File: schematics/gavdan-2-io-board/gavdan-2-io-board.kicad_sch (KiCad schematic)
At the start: 13 parts, among them J1 DB9_Female, U1 74LS04, U2 74LS133, U3 74LS08, U4 74LS08, U5 6551 ACIA, U6 MAX233CPP, U7 6522 VIA, Y1 1.8432MHZ

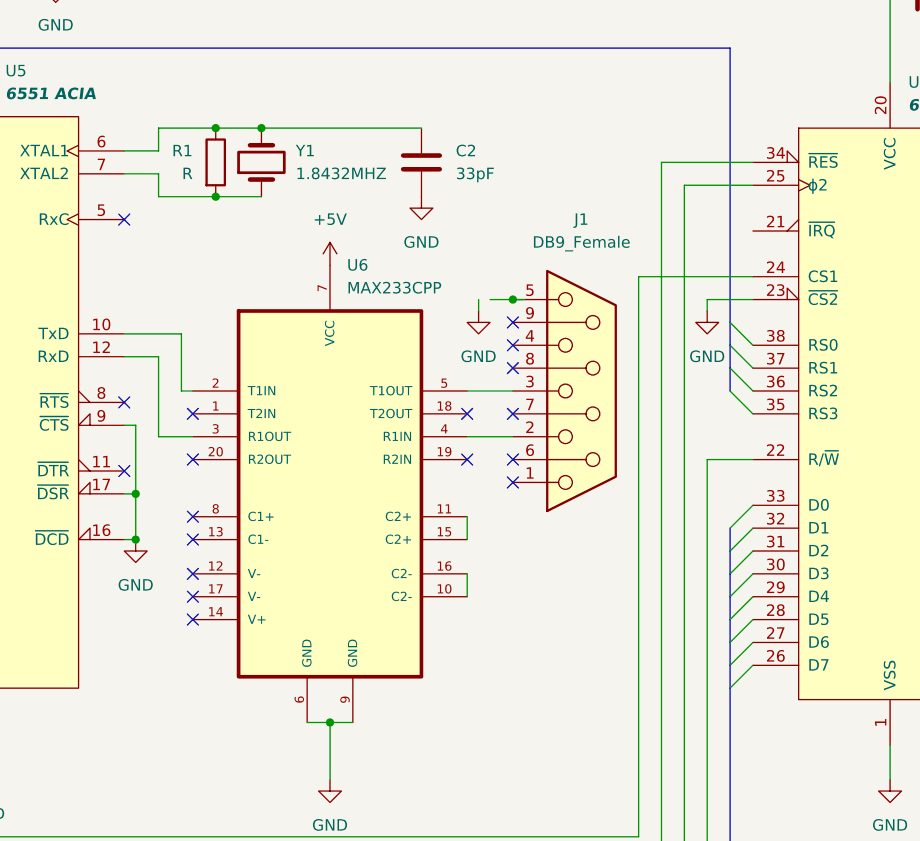
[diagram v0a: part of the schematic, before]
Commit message: Minor errors on schematics corrected
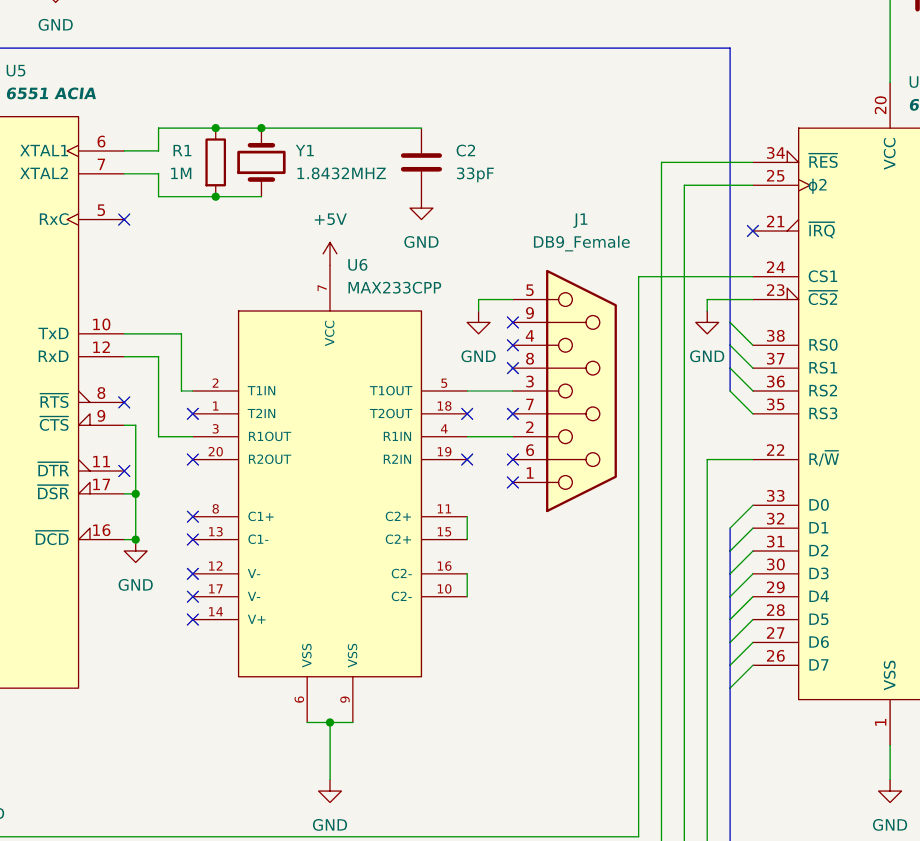
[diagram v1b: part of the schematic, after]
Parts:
- R1: value R -> 1M
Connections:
- net GND: now also J1.5
- no-connect marks 31 -> 32
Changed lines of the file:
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@@
   (junction (at 175.26 45.72) (diameter 0) (color 0 0 0 0)
-  )
-  (junction (at 208.28 64.77) (diameter 0) (color 0 0 0 0)
   )
   (junction (at 129.54 135.89) (diameter 0) (color 0 0 0 0)
@@
   (no_connect (at 165.1 76.2))
   (no_connect (at 165.1 55.88))
+  (no_connect (at 234.95 57.15))
   (no_connect (at 208.28 85.09))
   (no_connect (at 208.28 72.39))
@@
     (stroke (width 0) (type default) (color 0 0 0 0))
   )
-  (wire (pts (xy 208.28 64.77) (xy 209.55 64.77))
-    (stroke (width 0) (type default) (color 0 0 0 0))
-  )
   (bus (pts (xy 41.91 39.37) (xy 41.91 36.83))
     (stroke (width 0) (type default) (color 0 0 0 0))
@@
     (stroke (width 0) (type default) (color 0 0 0 0))
   )
+  (wire (pts (xy 208.28 64.77) (xy 204.47 64.77))
+    (stroke (width 0) (type default) (color 0 0 0 0))
+  )
   (bus (pts (xy 30.48 180.34) (xy 30.48 176.53))
     (stroke (width 0) (type default) (color 0 0 0 0))
@@
     (stroke (width 0) (type default) (color 0 0 0 0))
   )
-  (wire (pts (xy 205.74 64.77) (xy 208.28 64.77))
-    (stroke (width 0) (type default) (color 0 0 0 0))
-  )
   (wire (pts (xy 44.45 110.49) (xy 77.47 110.49))
     (stroke (width 0) (type default) (color 0 0 0 0))
@@
     (stroke (width 0) (type default) (color 0 0 0 0))
   )
+  (wire (pts (xy 204.47 64.77) (xy 204.47 66.04))
+    (stroke (width 0) (type default) (color 0 0 0 0))
+  )
   (wire (pts (xy 44.45 115.57) (xy 77.47 115.57))
     (stroke (width 0) (type default) (color 0 0 0 0))
@@
   )
   (bus (pts (xy 30.48 83.82) (xy 30.48 87.63))
-    (stroke (width 0) (type default) (color 0 0 0 0))
-  )
-  (wire (pts (xy 204.47 66.04) (xy 204.47 64.77))
     (stroke (width 0) (type default) (color 0 0 0 0))
   )
@@
       (effects (font (size 1.27 1.27)) (justify right))
     )
-    (property "Value" "R" (id 1) (at 172.72 50.7999 0)
+    (property "Value" "1M" (id 1) (at 172.72 50.7999 0)
       (effects (font (size 1.27 1.27)) (justify right))
     )
@@
     )
     (path "/91bc8827-3474-4406-866c-90ffdcf01241"
-      (reference "R1") (unit 1) (value "R") (footprint "")
+      (reference "R1") (unit 1) (value "1M") (footprint "")
     )
     (path "/e349a370-d956-4396-bf48-f79433bb1b93"

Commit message: Corrected error with reversed CS lines
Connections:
- net at U5.2 (CS1): now also U4.8; no longer U3.8
- net at U7.24 (CS1): now also U3.8; no longer U4.8
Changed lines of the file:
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@@
-    (stroke (width 0) (type default) (color 0 0 0 0))
-  )
-  (wire (pts (xy 222.25 62.23) (xy 222.25 124.46))
     (stroke (width 0) (type default) (color 0 0 0 0))
   )
@@
     (stroke (width 0) (type default) (color 0 0 0 0))
   )
-  (wire (pts (xy 134.62 110.49) (xy 134.62 124.46))
-    (stroke (width 0) (type default) (color 0 0 0 0))
-  )
   (bus (pts (xy 30.48 72.39) (xy 30.48 76.2))
     (stroke (width 0) (type default) (color 0 0 0 0))
   )
-  (wire (pts (xy 134.62 124.46) (xy 222.25 124.46))
+  (wire (pts (xy 119.38 124.46) (xy 222.25 124.46))
     (stroke (width 0) (type default) (color 0 0 0 0))
   )
@@
     (stroke (width 0) (type default) (color 0 0 0 0))
   )
+  (wire (pts (xy 116.84 85.09) (xy 119.38 85.09))
+    (stroke (width 0) (type default) (color 0 0 0 0))
+  )
   (bus (pts (xy 30.48 34.29) (xy 30.48 38.1))
     (stroke (width 0) (type default) (color 0 0 0 0))
@@
     (stroke (width 0) (type default) (color 0 0 0 0))
   )
+  (wire (pts (xy 121.92 60.96) (xy 121.92 110.49))
+    (stroke (width 0) (type default) (color 0 0 0 0))
+  )
   (wire (pts (xy 224.79 49.53) (xy 234.95 49.53))
     (stroke (width 0) (type default) (color 0 0 0 0))
@@
     (stroke (width 0) (type default) (color 0 0 0 0))
   )
-  (wire (pts (xy 121.92 60.96) (xy 121.92 85.09))
-    (stroke (width 0) (type default) (color 0 0 0 0))
-  )
   (bus (pts (xy 41.91 39.37) (xy 41.91 36.83))
     (stroke (width 0) (type default) (color 0 0 0 0))
@@
     (stroke (width 0) (type default) (color 0 0 0 0))
   )
-  (wire (pts (xy 121.92 85.09) (xy 116.84 85.09))
-    (stroke (width 0) (type default) (color 0 0 0 0))
-  )
   (wire (pts (xy 44.45 64.77) (xy 62.23 64.77))
     (stroke (width 0) (type default) (color 0 0 0 0))
@@
     (stroke (width 0) (type default) (color 0 0 0 0))
   )
-  (wire (pts (xy 116.84 110.49) (xy 134.62 110.49))
-    (stroke (width 0) (type default) (color 0 0 0 0))
-  )
   (wire (pts (xy 58.42 80.01) (xy 58.42 77.47))
     (stroke (width 0) (type default) (color 0 0 0 0))
@@
     (stroke (width 0) (type default) (color 0 0 0 0))
   )
+  (wire (pts (xy 222.25 124.46) (xy 222.25 62.23))
+    (stroke (width 0) (type default) (color 0 0 0 0))
+  )
   (bus (pts (xy 41.91 82.55) (xy 41.91 87.63))
     (stroke (width 0) (type default) (color 0 0 0 0))
@@
     (stroke (width 0) (type default) (color 0 0 0 0))
   )
+  (wire (pts (xy 116.84 110.49) (xy 121.92 110.49))
+    (stroke (width 0) (type default) (color 0 0 0 0))
+  )
   (wire (pts (xy 134.62 48.26) (xy 124.46 48.26))
     (stroke (width 0) (type default) (color 0 0 0 0))
@@
   )
   (bus (pts (xy 232.41 36.83) (xy 232.41 67.31))
+    (stroke (width 0) (type default) (color 0 0 0 0))
+  )
+  (wire (pts (xy 119.38 85.09) (xy 119.38 124.46))
     (stroke (width 0) (type default) (color 0 0 0 0))
   )
@@
     (effects (font (size 1.27 1.27)) (justify left bottom))
   )
-  (text "SEL BFEC-BFEF" (at 105.41 116.84 0)
-    (effects (font (size 1.27 1.27)) (justify left bottom))
-  )
-  (text "SEL BFF0-BFFF" (at 105.41 91.44 0)
-    (effects (font (size 1.27 1.27)) (justify left bottom))
-  )
+  (text "SEL BFEC-BFEF" (at 101.6 116.84 0)
+    (effects (font (size 1.27 1.27)) (justify left bottom))
+  )
+  (text "SEL BFF0-BFFF" (at 101.6 91.44 0)
+    (effects (font (size 1.27 1.27)) (justify left bottom))
+  )
